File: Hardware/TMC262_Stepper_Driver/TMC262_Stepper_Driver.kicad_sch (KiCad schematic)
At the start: 103 parts, among them J1 Conn_01x04, J3 629722000214, J4 Conn_01x02, J5 Conn_01x04, J6 Conn_01x05, Q1 SQJ504EP, Q2 SQJ504EP, Q3 SQJ504EP, Q4 SQJ504EP, SW1 SW_Push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

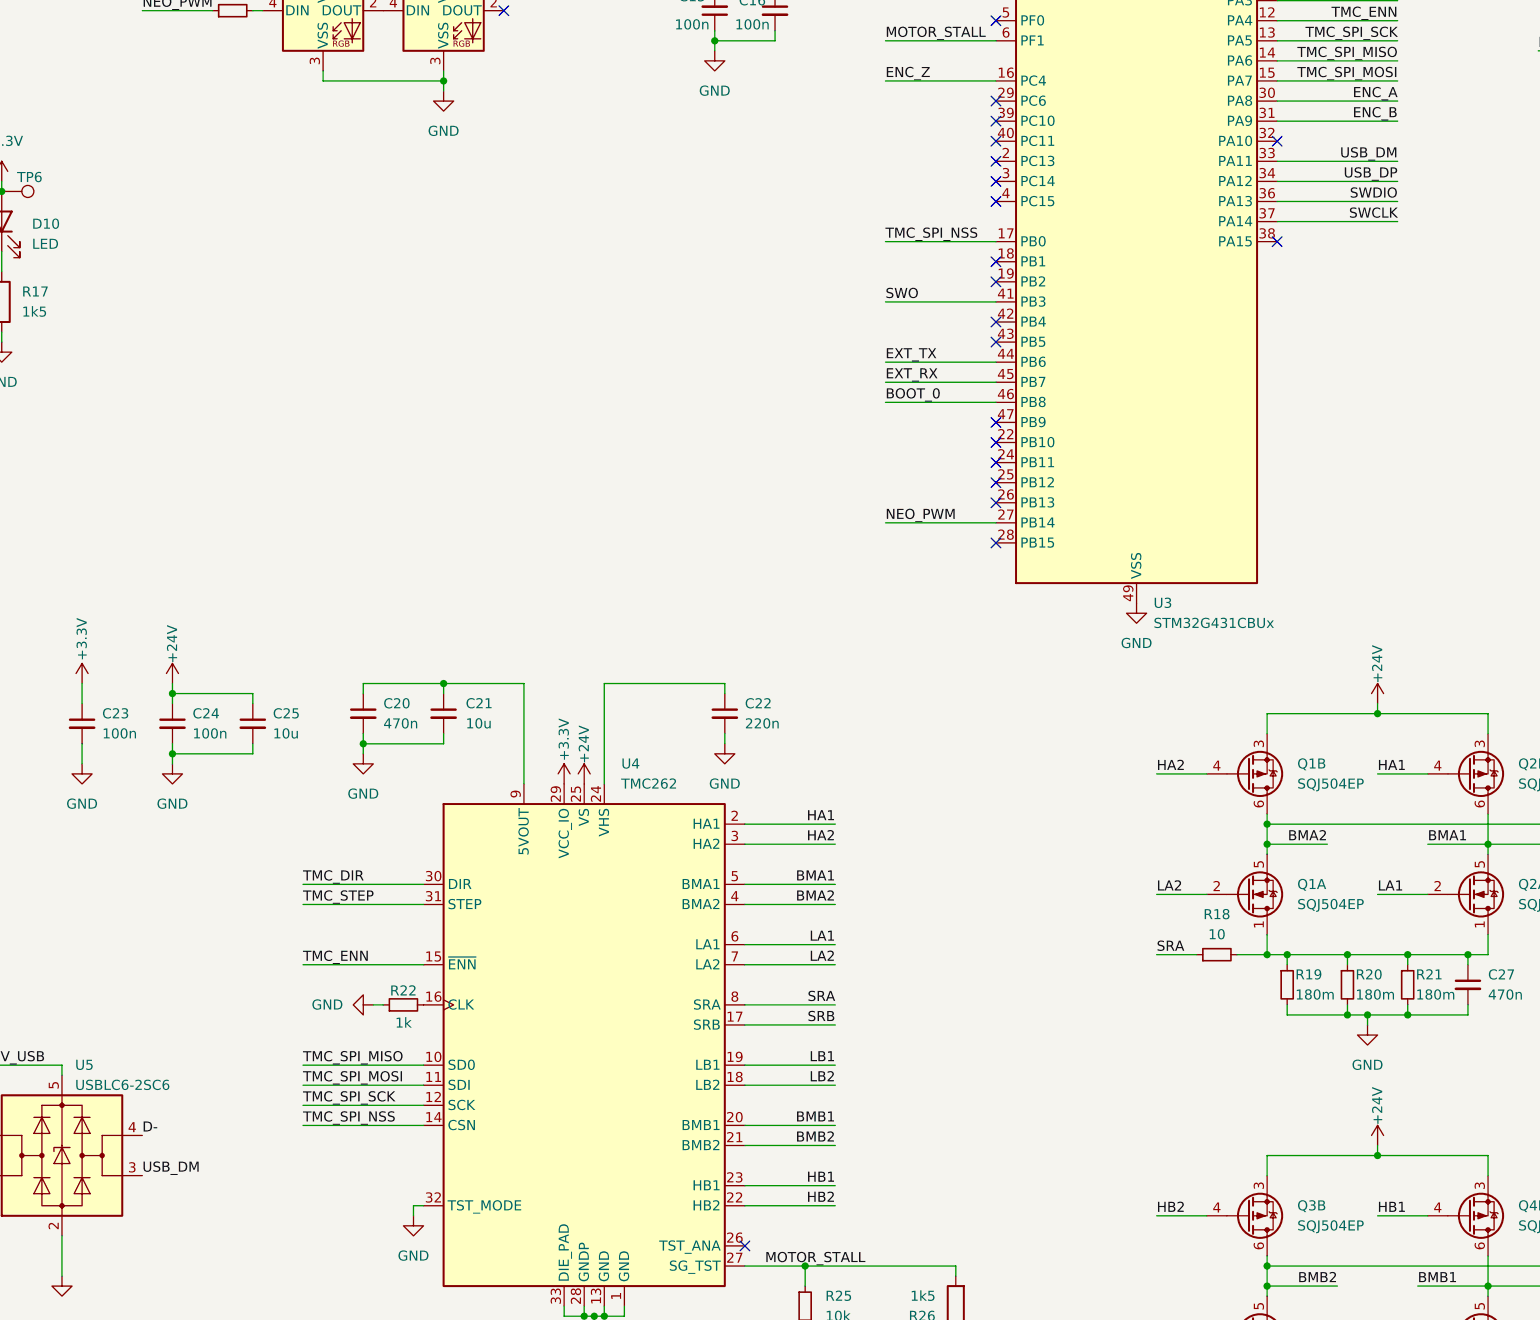
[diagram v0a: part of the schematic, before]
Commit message: tune length usb, add teardrops
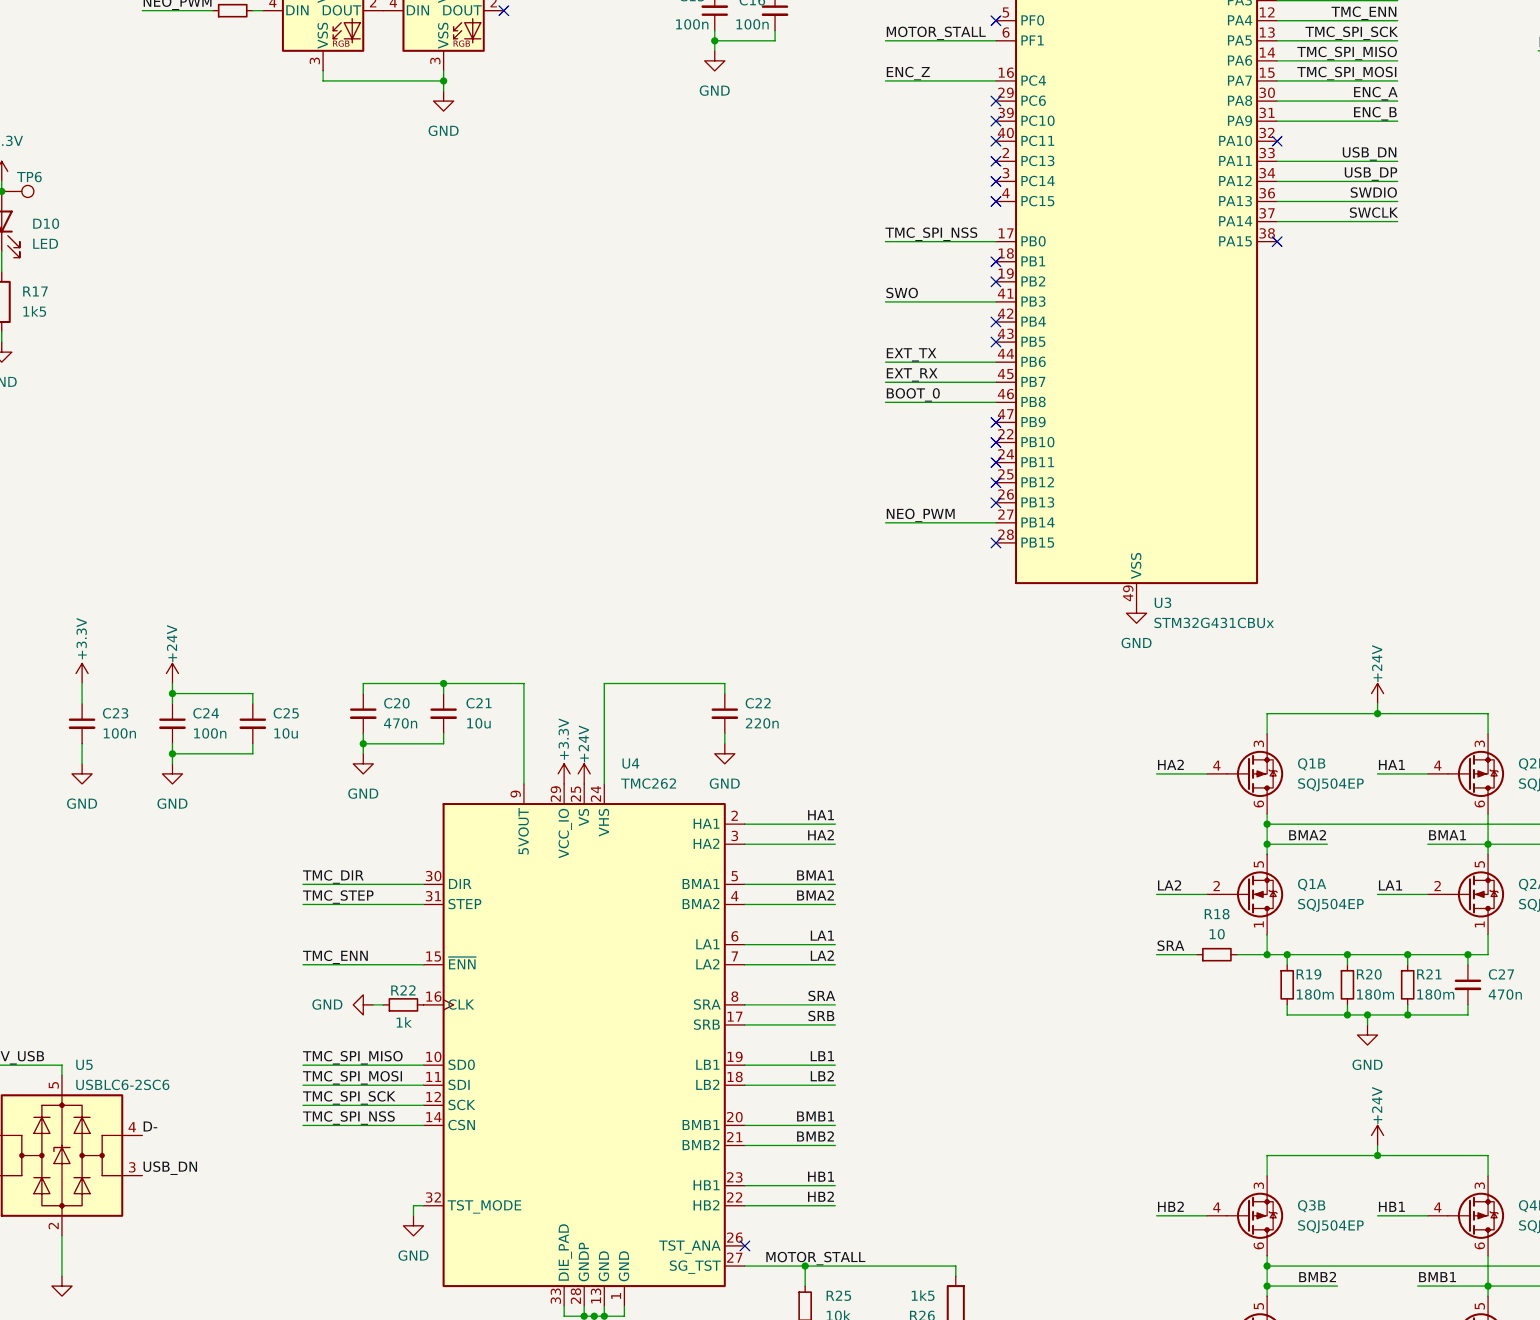
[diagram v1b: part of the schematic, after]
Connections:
- net USB_DM renamed USB_DN
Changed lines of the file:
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@@
 		)
 	)
-	(label "USB_DM"
+	(label "USB_DN"
 		(at 168.91 209.55 0)
 		(effects
@@
 		)
 	)
-	(label "USB_DM"
+	(label "USB_DN"
 		(at 327.66 81.28 180)
 		(effects

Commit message: generate bom
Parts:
- C11: MPN 885 012 107 006 -> WE 885012107006
- C12, C21: MPN 885 012 106 006 -> WE 885012106006
- C13: MPN 885 012 107 011 -> WE 885012107011
- C25, C26, C28: MPN 885 012 208 069 -> WE 885012208069
- C30: value C_Polarized_Small -> 220u; MPN 865060657012 -> WE 865060657012
- C7, C8: MPN 885012209048 -> WE 885012209048
- D1, D2: MPN (none) -> WS2812B
- D10, D13, D5, D6, D7, D8, D9: MPN (none) -> 150060RS55040
- D11, D12, D4: MPN (none) -> FSV340AF
- H1, H2, H3, H4, JP1: now in the parts list
- J3: MPN 629722000214 -> WE 629722000214
- R19, R20, R21, R28, R29, R30: MPN 561 070 332 057 -> WE 561070332057
- TP1, TP2, TP3, TP4, TP5, TP6: now left out of the parts list
- U1: MPN (none) -> AZ1117CH-3.3TRG1
- U2: MPN (none) -> WE 171013801
- U3: MPN (none) -> STM32G431CBU6
- U4: MPN (none) -> TMC262C-LA
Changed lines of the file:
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@@
 			)
 		)
+		(property "MPN" "WE 171013801"
+			(at 72.39 43.18 0)
+			(effects
+				(font
+					(size 1.27 1.27)
+				)
+			)
+		)
 		(pin "7"
 		)
@@
 		(unit 1)
 		(exclude_from_sim no)
-		(in_bom yes)
+		(in_bom no)
 		(on_board yes)
 		(dnp no)
@@
 		(unit 1)
 		(exclude_from_sim no)
-		(in_bom yes)
+		(in_bom no)
 		(on_board yes)
 		(dnp no)
@@
 			)
 		)
+		(property "MPN" "150060RS55040"
+			(at 151.13 88.9 0)
+			(effects
+				(font
+					(size 1.27 1.27)
+				)
+				(hide yes)
+			)
+		)
 		(pin "1"
 		)
@@
 			)
 		)
-		(property "MPN" "561 070 332 057"
+		(property "MPN" "WE 561070332057"
 			(at 328.93 185.42 0)
 			(effects
@@
 			)
 		)
+		(property "MPN" "150060RS55040"
+			(at 107.95 88.9 0)
+			(effects
+				(font
+					(size 1.27 1.27)
+				)
+				(hide yes)
+			)
+		)
 		(pin "1"
 		)
@@
 			)
 		)
-		(property "MPN" "885 012 106 006"
+		(property "MPN" "WE 885012106006"
 			(at 207.01 151.13 0)
 			(effects
@@
 			)
 		)
+		(property "MPN" "WS2812B"
+			(at 191.77 62.23 0)
+			(effects
+				(font
+					(size 1.27 1.27)
+				)
+				(hide yes)
+			)
+		)
 		(pin "2"
 		)
@@
 			)
 		)
-		(property "MPN" "885 012 208 069"
+		(property "MPN" "WE 885012208069"
 			(at 182.88 152.4 0)
 			(effects
@@
 			)
 		)
+		(property "MPN" "150060RS55040"
+			(at 130.81 88.9 0)
+			(effects
+				(font
+					(size 1.27 1.27)
+				)
+				(hide yes)
+			)
+		)
 		(pin "1"
 		)
@@
 			)
 		)
-		(property "MPN" "885 012 107 006"
+		(property "MPN" "WE 885012107006"
 			(at 99.06 45.72 0)
 			(effects
@@
 		(unit 1)
 		(exclude_from_sim yes)
-		(in_bom no)
+		(in_bom yes)
 		(on_board yes)
 		(dnp no)
@@
 			)
 		)
-		(property "MPN" "561 070 332 057"
+		(property "MPN" "WE 561070332057"
 			(at 320.04 241.3 0)
 			(effects
@@
 		(unit 1)
 		(exclude_from_sim yes)
-		(in_bom no)
+		(in_bom yes)
 		(on_board yes)
 		(dnp no)
@@
 		(unit 1)
 		(exclude_from_sim no)
-		(in_bom yes)
+		(in_bom no)
 		(on_board yes)
 		(dnp no)
@@
 			)
 		)
-		(property "MPN" "561 070 332 057"
+		(property "MPN" "WE 561070332057"
 			(at 321.31 185.42 0)
 			(effects
@@
 			)
 		)
-		(property "MPN" "885 012 208 069"
+		(property "MPN" "WE 885012208069"
 			(at 368.3 166.37 0)
 			(effects
@@
 			)
 		)
+		(property "MPN" "150060RS55040"
+			(at 119.38 88.9 0)
+			(effects
+				(font
+					(size 1.27 1.27)
+				)
+				(hide yes)
+			)
+		)
 		(pin "1"
 		)
@@
 			)
 		)
+		(property "MPN" "TMC262C-LA"
+			(at 224.79 193.04 0)
+			(effects
+				(font
+					(size 1.27 1.27)
+				)
+				(hide yes)
+			)
+		)
 		(pin "4"
 		)
@@
 			)
 		)
+		(property "MPN" "AZ1117CH-3.3TRG1"
+			(at 140.97 41.91 0)
+			(effects
+				(font
+					(size 1.27 1.27)
+				)
+				(hide yes)
+			)
+		)
 		(pin "3"
 		)
@@
 			)
 		)
-		(property "MPN" "561 070 332 057"
+		(property "MPN" "WE 561070332057"
 			(at 327.66 241.3 0)
 			(effects
@@
 			)
 		)
+		(property "MPN" "WS2812B"
+			(at 207.01 62.23 0)
+			(effects
+				(font
+					(size 1.27 1.27)
+				)
+				(hide yes)
+			)
+		)
 		(pin "2"
 		)
@@
 			)
 		)
-		(property "MPN" "561 070 332 057"
+		(property "MPN" "WE 561070332057"
 			(at 312.42 241.3 0)
 			(effects
@@
 		(unit 1)
 		(exclude_from_sim yes)
-		(in_bom no)
+		(in_bom yes)
 		(on_board yes)
 		(dnp no)
@@
 		(unit 1)
 		(exclude_from_sim yes)
-		(in_bom no)
+		(in_bom yes)
 		(on_board yes)
 		(dnp no)
@@
 			)
 		)
+		(property "MPN" "150060RS55040"
+			(at 96.52 88.9 0)
+			(effects
+				(font
+					(size 1.27 1.27)
+				)
+				(hide yes)
+			)
+		)
 		(pin "1"
 		)
@@
 		(unit 1)
 		(exclude_from_sim no)
-		(in_bom yes)
+		(in_bom no)
 		(on_board yes)
 		(dnp no)
@@
 		(unit 1)
 		(exclude_from_sim yes)
-		(in_bom no)
+		(in_bom yes)
 		(on_board yes)
 		(dnp no)
@@
 			)
 		)
+		(property "MPN" "150060RS55040"
+			(at 140.97 88.9 0)
+			(effects
+				(font
+					(size 1.27 1.27)
+				)
+				(hide yes)
+			)
+		)
 		(pin "1"
 		)
@@
 			)
 		)
+		(property "MPN" "150060RS55040"
+			(at 271.78 236.22 0)
+			(effects
+				(font
+					(size 1.27 1.27)
+				)
+				(hide yes)
+			)
+		)
 		(pin "1"
 		)
@@
 			)
 		)
-		(property "MPN" "885 012 208 069"
+		(property "MPN" "WE 885012208069"
 			(at 368.3 220.98 0)
 			(effects
@@
 			)
 		)
-		(property "MPN" "885 012 106 006"
+		(property "MPN" "WE 885012106006"
 			(at 132.08 46.99 0)
 			(effects
@@
 			)
 		)
-		(property "MPN" "885 012 107 011"
+		(property "MPN" "WE 885012107011"
 			(at 149.86 46.99 0)
 			(effects
@@
 			)
 		)
+		(property "MPN" "FSV340AF"
+			(at 63.5 99.06 0)
+			(effects
+				(font
+					(size 1.27 1.27)
+				)
+			)
+		)
 		(pin "2"
 		)
@@
 			)
 		)
-		(property "Value" "C_Polarized_Small"
+		(property "Value" "220u"
 			(at 69.85 258.5338 0)
 			(effects
@@
 			)
 		)
-		(property "MPN" "865060657012"
+		(property "MPN" "WE 865060657012"
 			(at 67.31 257.81 0)
 			(effects
@@
 			)
 		)
-		(property "MPN" "561 070 332 057"
+		(property "MPN" "WE 561070332057"
 			(at 313.69 185.42 0)
 			(effects
@@
 			)
 		)
+		(property "MPN" "FSV340AF"
+			(at 63.5 83.82 0)
+			(effects
+				(font
+					(size 1.27 1.27)
+				)
+			)
+		)
 		(pin "2"
 		)
@@
 		(unit 1)
 		(exclude_from_sim no)
-		(in_bom yes)
+		(in_bom no)
 		(on_board yes)
 		(dnp no)
@@
 		(unit 1)
 		(exclude_from_sim no)
-		(in_bom yes)
+		(in_bom no)
 		(on_board yes)
 		(dnp no)
@@
 			)
 		)
-		(property "MPN" "629722000214"
+		(property "MPN" "WE 629722000214"
 			(at 123.19 209.55 0)
 			(effects
@@
 			)
 		)
-		(property "MPN" "885012209048"
+		(property "MPN" "WE 885012209048"
 			(at 34.29 39.37 0)
 			(effects
@@
 			)
 		)
+		(property "MPN" "FSV340AF"
+			(at 63.5 91.44 0)
+			(effects
+				(font
+					(size 1.27 1.27)
+				)
+			)
+		)
 		(pin "2"
 		)
@@
 			)
 		)
-		(property "MPN" "885012209048"
+		(property "MPN" "WE 885012209048"
 			(at 43.18 39.37 0)
 			(effects
@@
 			)
 		)
+		(property "MPN" "STM32G431CBU6"
+			(at 294.64 91.44 0)
+			(effects
+				(font
+					(size 1.27 1.27)
+				)
+			)
+		)
